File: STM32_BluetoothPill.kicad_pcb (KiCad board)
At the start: 2 copper layers, 25 x 75 mm, 45 parts, among them J1 USB_A, J2 Conn, J3 Conn, J4 Conn, J5 RFShield, SW1 Reset, SW2 User PB, U1 STM32WBxx, U2 USBLC6-2SC6, U3 LD3985M33R_SOT23, Y1 8M, Y2 32k768

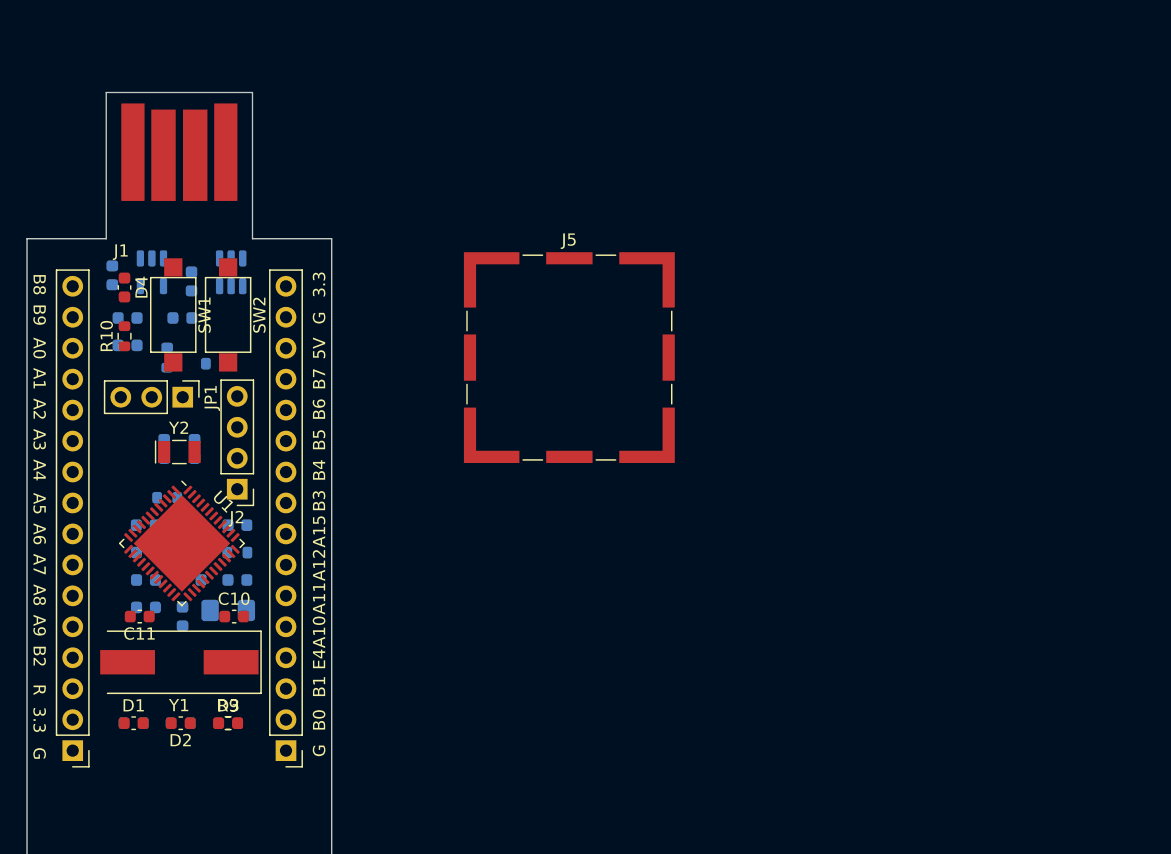
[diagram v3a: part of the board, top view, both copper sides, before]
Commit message: matched low pass filter added
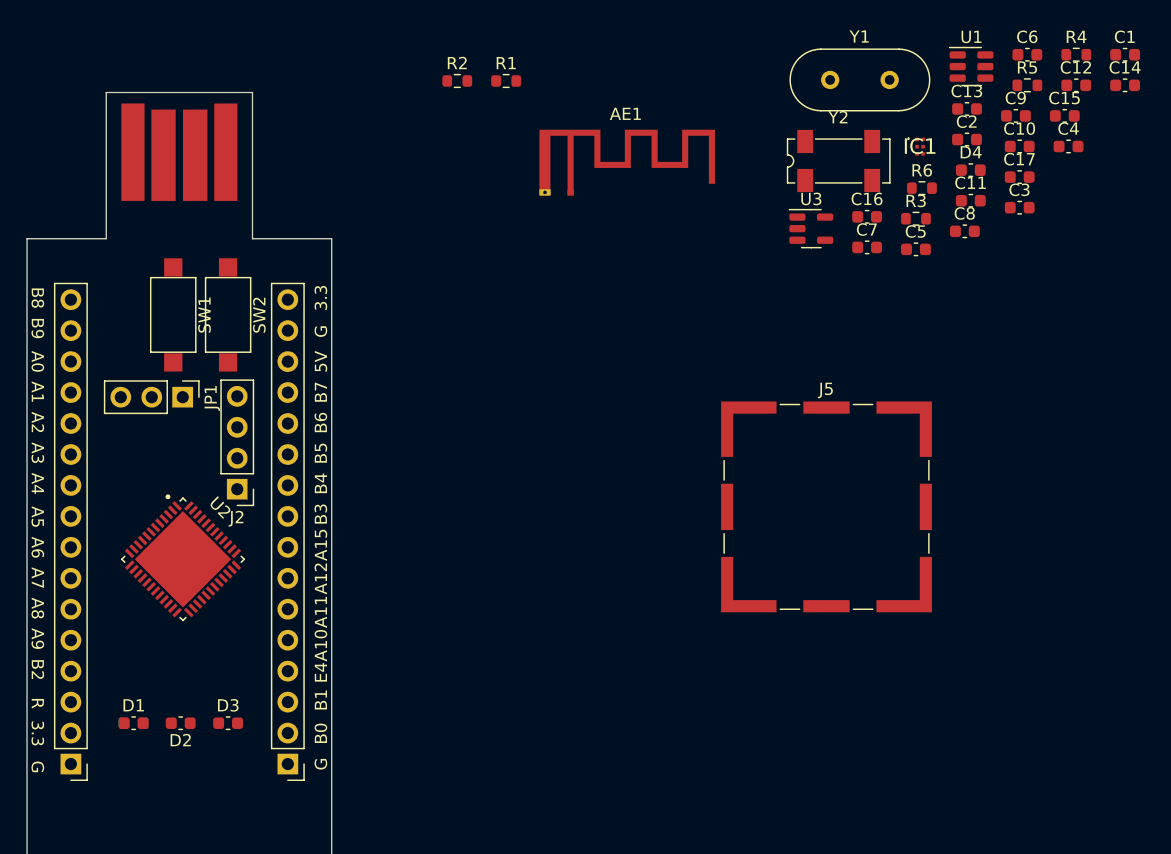
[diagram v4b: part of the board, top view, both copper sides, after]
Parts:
- removed C18, C19: 100n, Capacitor_SMD:C_0603_1608Metric
- removed L1: 10u, Inductor_SMD:L_1206_3216Metric_Pad1.42x1.75mm_HandSolder
- removed R10, R8, R9: 680, Resistor_SMD:R_0603_1608Metric
- added AE1: Antenna_Shield, RF_Antenna:Texas_SWRA117D_2.4GHz_Right, F.Cu at (74.6, 26.2)
- added IC1: MLPF-WB-01E3, lib:MLPFWB01E3, F.Cu at (103.3, 22.4)
- added R1: R_Small, Resistor_SMD:R_0603_1608Metric, F.Cu at (69.3, 17.1)
- added R2: R_Small, Resistor_SMD:R_0603_1608Metric, F.Cu at (65.3, 17.1)
- C1, C15, C2, C3, C4, C5, C7: value 100n -> C_Small; moved to F.Cu
- C10, C11: value 12p -> C_Small
- C12, C13: value 10p -> C_Small; moved to F.Cu
- C14, C17: value 1u -> C_Small; moved to F.Cu
- C16: value 10n -> C_Small; moved to F.Cu
- C6, C9: value 4.7u -> C_Small; moved to F.Cu
- C8: value 100p -> C_Small; moved to F.Cu
- D1: value GRN -> LED_Small
- D2: value RED -> LED_Small
- D3: value BLU -> LED_Small
- D4: value PWR -> LED_Small
- J2: value Conn -> Conn_01x04
- J3, J4: value Conn -> Conn_01x16
- J5: value RFShield -> RFShield_OnePiece
- R3: value NC -> R_Small; moved to F.Cu
- R4: value 0 -> R_Small; moved to F.Cu
- R5: value 10k -> R_Small; moved to F.Cu
- R6: value 1k -> R_Small; moved to F.Cu
- R7: value 680 -> R_Small
- SW1: value Reset -> SW_Push
- SW2: value User PB -> SW_Push
- U1: value STM32WBxx -> USBLC6-2SC6; footprint Package_DFN_QFN:QFN-48-1EP_7x7mm_P0.5mm_EP5.6x5.6mm -> Package_TO_SOT_SMD:SOT-23-6
- U2: value USBLC6-2SC6 -> STM32WB55CEU6TR; footprint Package_TO_SOT_SMD:SOT-23-6 -> lib:QFN50P700X700X60-49N; moved to F.Cu
- U3: moved to F.Cu
- Y1: value 8M -> Crystal_Small; footprint Crystal:Crystal_SMD_HC49-SD -> Crystal:Crystal_HC49-4H_Vertical
- Y2: value 32k768 -> Crystal_Small; footprint Crystal:Crystal_SMD_G8-2Pin_3.2x1.5mm -> Crystal:Crystal_SMD_SeikoEpson_MC306-4Pin_8.0x3.2mm
- moved C1 90.0 mm to (120.1, 14.9), turned to 0 degrees
- moved C4 82.7 mm to (115.5, 22.4), turned to 0 degrees
- moved C12 80.6 mm to (116.1, 17.4), turned to 0 degrees
- moved C6 79.8 mm to (112.1, 14.9)
- moved C15 79.2 mm to (115.2, 19.9), turned to 0 degrees
- moved R4 78.6 mm to (116.1, 14.9), turned to 0 degrees
- moved R5 78.3 mm to (112.1, 17.4), turned to 0 degrees
- moved C14 78.3 mm to (120.1, 17.4), turned to 0 degrees
- moved C11 76.2 mm to (107.4, 26.9), turned to 0 degrees
- moved U1 75.7 mm to (107.5, 15.9), turned to 0 degrees
- moved C10 75.1 mm to (111.5, 22.4)
- moved C17 74.5 mm to (111.5, 24.9), turned to 0 degrees
- moved C3 74.5 mm to (111.5, 27.4)
- moved C9 74.4 mm to (111.1, 19.9), turned to 0 degrees
- moved C8 73.0 mm to (107.0, 29.4)
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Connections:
- C1 pad 1: +3V3 -> +3.3V
- C12 pad 1: Net-(C12-Pad1) -> +5V
- C13 pad 1: Net-(C13-Pad1) -> +5V
- C14 pad 1: +5V -> Net-(C14-Pad1)
- C15 pad 1: +5V -> Net-(C15-Pad1)
- C16 pad 1: Net-(C16-Pad1) -> Net-(C15-Pad1)
- C17 pad 1: Net-(C17-Pad1) -> RESET
- C2 pad 1: +3V3 -> +3.3V
- C3 pad 1: +3V3 -> +3.3V
- C4 pad 1: +3V3 -> +3.3V
- C5 pad 1: +3V3 -> +3.3V
- C6 pad 1: +3V3 -> +3.3V
- C7 pad 1: GND -> +3.3V
- C7 pad 2: +3V3 -> GND
- C8 pad 1: GND -> Net-(C8-Pad1)
- C8 pad 2: +3V3 -> GND
- C9 pad 1: GND -> Net-(C9-Pad1)
- C9 pad 2: Net-(C9-Pad2) -> GND
- J2 pad 1: +3V3 -> +3.3V
- J3 pad 2: +3V3 -> +3.3V
- J4 pad 16: +3V3 -> +3.3V
- JP1 pad 1: +3V3 -> +3.3V
- R3 pad 1: Net-(C9-Pad2) -> PA10
- R3 pad 2: +3V3 -> Net-(R3-Pad2)
- R4 pad 1: +3V3 -> PB0
- R4 pad 2: Net-(C17-Pad1) -> Net-(D1-Pad2)
- R5 pad 1: +3V3 -> PB1
- R5 pad 2: RESET -> Net-(D2-Pad2)
- R6 pad 1: PA10 -> PE4
- R6 pad 2: Net-(R6-Pad2) -> Net-(D3-Pad2)
- R7 pad 1: PB0 -> +3.3V
- R7 pad 2: Net-(D1-Pad2) -> Net-(D4-Pad2)
- SW2 pad 2: Net-(R6-Pad2) -> Net-(R3-Pad2)
- U1 pad 1: unconnected-(U1-Pad1) -> /D-
- U1 pad 2: Net-(C13-Pad1) -> GND
- U1 pad 3: Net-(C12-Pad1) -> /D+
- U1 pad 4: Net-(JP1-Pad2) -> USB_P
- U1 pad 5: PB8 -> +5V
- U1 pad 6: PB9 -> USB_N
- U2 pad 1: /D- -> unconnected-(U2-Pad1)
- U2 pad 2: GND -> Net-(C11-Pad1)
- U2 pad 3: /D+ -> Net-(C10-Pad1)
- U2 pad 4: USB_P -> Net-(JP1-Pad2)
- U2 pad 5: +5V -> PB8
- U2 pad 6: USB_N -> PB9
- U3 pad 4: Net-(C16-Pad1) -> Net-(C14-Pad1)
- U3 pad 5: Net-(C17-Pad1) -> Net-(C15-Pad1)
- Y1 pad 1: Net-(C10-Pad1) -> Net-(C8-Pad1)
- Y1 pad 2: Net-(C11-Pad1) -> Net-(C9-Pad1)
- Y2 pad 1: Net-(C12-Pad1) -> Net-(C10-Pad1)
- Y2 pad 2: Net-(C13-Pad1) -> Net-(C11-Pad1)

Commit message: pcb first try
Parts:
- removed AE1: Antenna_Shield, RF_Antenna:Texas_SWRA117D_2.4GHz_Right
- removed J5: RFShield_OnePiece, RF_Shielding:Laird_Technologies_BMI-S-202-F_16.50x16.50mm
- C1, C10, C11, C12, C13, C14, C15, C16, C17, C2, C3, C4, C5, C6, C7, C8, C9, R1, R2, R3, R4, R5, R6, U1, U3: moved to B.Cu
- STM32: renamed from U2; footprint lib:QFN50P700X700X60-49N -> Package_DFN_QFN:QFN-48-1EP_7x7mm_P0.5mm_EP5.45x5.45mm
- moved R4 89.7 mm to (48.1, 73.4), turned to -90 degrees
- moved C9 87.1 mm to (39.7, 69.7), turned to 180 degrees
- moved R5 86.8 mm to (45.8, 73.4), turned to -90 degrees
- moved C1 85.2 mm to (48.2, 60.6), turned to 90 degrees
- moved IC1 82.6 mm to (38.4, 73.6), turned to 180 degrees
- moved C14 82.2 mm to (40.6, 38.2), turned to -90 degrees
- moved C6 81.7 mm to (46.6, 63.7), turned to -90 degrees
- moved C15 79.2 mm to (37.9, 37.5), turned to 180 degrees
- moved C2 77.1 mm to (37.1, 54.1), turned to 180 degrees
- moved R6 76.4 mm to (43.6, 73.4), turned to -90 degrees
- moved C12 75.6 mm to (42.3, 33.8), turned to -90 degrees
- moved C4 75.5 mm to (46.3, 52.8)
- moved C10 73.6 mm to (41.9, 46.6), turned to 90 degrees
- moved C8 73.0 mm to (46.1, 69.7)
- moved C13 71.7 mm to (36.9, 33.8), turned to -90 degrees
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- renumbered JP1 to BOOT, J2 to DBG, SW2 to PA10, D1 to PB0, D2 to PB1, D3 to PE4, D4 to PWR, SW1 to RESET
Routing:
- net GND: track 0.00 -> 173.1 mm, vias 0 -> 9
- net +3.3V: track 0.00 -> 104.0 mm, vias 0 -> 8
- net RESET: track 0.00 -> 49.9 mm, vias 0 -> 4
- net +5V: track 0.00 -> 38.2 mm, vias 0 -> 2
- net USB_N: track 0.00 -> 28.7 mm, vias 0 -> 1
- net USB_P: track 0.00 -> 24.8 mm, vias 0 -> 1
- net PB8: track 0.00 -> 24.0 mm, vias 0 -> 1
- net PA10: track 0.00 -> 22.7 mm, vias 0 -> 1
- net PB9: track 0.00 -> 21.8 mm, vias 0 -> 1
- net PE4: track 0.00 -> 21.3 mm
- net PA0: track 0.00 -> 19.9 mm
- net PB1: track 0.00 -> 19.4 mm
- net SWCLK: track 0.00 -> 18.2 mm, vias 0 -> 1
- net PB0: track 0.00 -> 17.5 mm
- net PA1: track 0.00 -> 17.4 mm
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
